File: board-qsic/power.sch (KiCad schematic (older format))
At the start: 43 parts, among them U306 AOZ3010PI, U307 AOZ3010PI, U308 RT8288A, U309 SC189, U401 XC7A75T-CSG324

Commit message: Reworked board from template.  Changed schematic to let me use the bus drivers and level converters more efficiently so to get all the signals.
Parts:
- removed C301, C302, C309, C310: 10uF, Capacitors_SMD:C_0603, symbol qsic-rescue:C_Small-device
- removed C303, C304: 2.2nF, Capacitors_SMD:C_0603, symbol qsic-rescue:C_Small-device
- removed C305, C306, C311, C312, C315, C317, C318, C320, C321, C323, C324, C326: 100nF, Capacitors_SMD:C_0603, symbol qsic-rescue:C_Small-device
- removed C307, C308, C313, C314: 22uF, Capacitors_SMD:C_0805, symbol qsic-rescue:C_Small-device
- removed D301: Configure, LEDs:LED-0603, symbol qsic-rescue:LED_Small_ALT
- removed L301, L302: 4.7uH, Resistors_SMD:R_0805, symbol qsic-rescue:L_Small-device
- removed L303: 1.5uH, Resistors_SMD:R_0805, symbol qsic-rescue:L_Small-device
- removed L304: 2.2uH, Resistors_SMD:R_0805, symbol qsic-rescue:L_Small-device
- removed R361: 240, Resistors_SMD:R_0603, symbol qsic-rescue:R-device
- removed R362, R363: 7.5k, Resistors_SMD:R_0603, symbol qsic-rescue:R-device
- removed R364: 31.1k, Resistors_SMD:R_0603, symbol qsic-rescue:R-device
- removed R365, R366: 10k, Resistors_SMD:R_0603, symbol qsic-rescue:R-device
- removed R367: 11.5k, Resistors_SMD:R_0603, symbol qsic-rescue:R-device
- removed R368: 100k, Resistors_SMD:R_0603, symbol qsic-rescue:R-device
- removed R369: 50k, Resistors_SMD:R_0603, symbol qsic-rescue:R-device
- removed R370: 18.2k, Resistors_SMD:R_0603, symbol qsic-rescue:R-device
- removed R371: 4.7k, Resistors_SMD:R_0603, symbol qsic-rescue:R-device
- removed U306, U307: AOZ3010PI, Housings_SOIC:SOIC-8-1EP_3.9x4.9mm_Pitch1.27mm, symbol myLib:AOZ3010PI
- removed U308: RT8288A, Housings_SOIC:SOIC-8-1EP_3.9x4.9mm_Pitch1.27mm, symbol myLib:RT8288A
- removed U309: SC189, TO_SOT_Packages_SMD:SOT-23-5, symbol myLib:SC189
- removed U401: XC7A75T-CSG324, myMods.pretty:CSG324, symbol myLib:XC7A75T-CSG324
- added C1201, C1203, C1205, C1207: 22uF, Capacitor_SMD:C_0805_2012Metric, symbol Device:CP1_Small
- added C1202, C1204, C1206, C1208: 10uF, Capacitor_SMD:C_0805_2012Metric, symbol Device:CP1_Small
- added R1201: 511k, Resistor_SMD:R_0603_1608Metric, symbol Device:R
- added R1202, R1205, R1208, R1211: 499k, Resistor_SMD:R_0603_1608Metric, symbol Device:R
- added R1203, R1206, R1209, R1212: 162k, Resistor_SMD:R_0603_1608Metric, symbol Device:R
- added R1204: 200k, Resistor_SMD:R_0603_1608Metric, symbol Device:R
- added R1207: 143k, Resistor_SMD:R_0603_1608Metric, symbol Device:R
- added R1210: 40.2, Resistor_SMD:R_0603_1608Metric, symbol Device:R
- added U101: XC7A75T-CSG324, Package_BGA:BGA-324_15.0x15.0mm_Layout18x18_P0.8mm_Ball0.5mm_Pad0.4mm_NSMD, symbol FPGA_Xilinx_Artix7:XC7A75T-CSG324
- added U1201, U1202, U1203, U1204: TPS82085, Package_LGA:Texas_SIL0008D_MicroSiP-8-1EP_2.8x3mm_P0.65mm_EP1.1x1.9mm_ThermalVias, symbol myLib:TPS82085
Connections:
- net labels added: 1V0, 1V5, 1V8, 3V3, 5V
- net labels removed: +1V0, +1V5, +1V8, +3V3, +5V
- wire segments 317 -> 240
- no-connect marks 4 -> 0
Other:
- note removed: "1.0V/4A"
- note removed: "1.5V/2A"
- note removed: "1.8V/1.5A"
- note removed: "3.3V/2A"

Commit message: Design of prototype is done.  Needs checking before sending out.
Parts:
- added C508, C512: 100nF, Capacitor_SMD:C_0603_1608Metric, symbol Device:C
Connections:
- net 1V0: now also C512.1
- net 1V8: now also C508.1
- net GND: now also U101.E8 (VCCBATT_0), C508.2, C512.2
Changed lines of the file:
@@
 $Descr A 11000 8500
 encoding utf-8
-Sheet 53 53
+Sheet 5 5
 Title "Power"
-Date "2019-09-30"
+Date "2019-10-07"
 Rev "0.2"
 Comp "QSIC - QBUS Storage & I/O Card"
@@
 $EndDescr
 Wire Wire Line
-	8875 1550 8875 1650
+	8875 1450 8875 1525
 Wire Wire Line
 	8775 1650 8875 1650
@@
 	6675 1950 6775 1950
 Wire Wire Line
-	6675 1600 6675 1650
+	6675 1425 6675 1525
 Wire Wire Line
 	6775 1650 6675 1650
@@
 Text HLabel 1125 1350 0    60   Input ~ 0
 5V
-Text Label 8875 1550 0    60   ~ 0
+Text Label 8875 1450 0    60   ~ 0
 1V0
-Text Label 6675 1600 2    60   ~ 0
+Text Label 6675 1425 2    60   ~ 0
 1V8
 Text HLabel 4050 1500 2    60   Output ~ 0
@@
 $EndComp
 Wire Wire Line
-	6775 2550 6700 2550
-Wire Wire Line
-	6700 2550 6700 2450
-Wire Wire Line
-	6775 2450 6700 2450
-Text Label 6575 2550 2    60   ~ 0
+	6775 2550 6750 2550
+Wire Wire Line
+	6750 2550 6750 2450
+Wire Wire Line
+	6775 2450 6750 2450
+Text Label 6700 2550 2    60   ~ 0
 1V0
 $Comp
@@
 	6475 2150 6775 2150
 Wire Wire Line
-	6575 2550 6700 2550
-Connection ~ 6700 2550
+	6700 2550 6750 2550
+Connection ~ 6750 2550
 $Comp
 L myLib:TPS82085 U1201
@@
 Connection ~ 1225 1500
 Connection ~ 1225 2750
+$Comp
+L Device:C C?
+U 1 1 5DDB3BFE
+P 9075 1700
+AR Path="/5DCB8CA6/5DDB3BFE" Ref="C?"  Part="1"
+AR Path="/5D96DF52/5DDB3BFE" Ref="C512"  Part="1"
+F 0 "C512" H 9190 1746 50  0000 L CNN
+F 1 "100nF" H 9190 1655 50  0000 L CNN
+F 2 "Capacitor_SMD:C_0603_1608Metric" H 9113 1550 50  0001 C CNN
+F 3 "~" H 9075 1700 50  0001 C CNN
+	1    9075 1700
+	1    0    0    -1
+$EndComp
+$Comp
+L Device:C C?
+U 1 1 5DDC711B
+P 6475 1700
+AR Path="/5DCB8CA6/5DDC711B" Ref="C?"  Part="1"
+AR Path="/5D96DF52/5DDC711B" Ref="C508"  Part="1"
+F 0 "C508" H 6361 1746 50  0000 R CNN
+F 1 "100nF" H 6361 1655 50  0000 R CNN
+F 2 "Capacitor_SMD:C_0603_1608Metric" H 6513 1550 50  0001 C CNN
+F 3 "~" H 6475 1700 50  0001 C CNN
+	1    6475 1700
+	1    0    0    -1
+$EndComp
+$Comp
+L power:GND #PWR?
+U 1 1 5DDDA595
+P 6475 1850
+AR Path="/5DCB8CA6/5DCBEACE/5DDDA595" Ref="#PWR?"  Part="1"
+AR Path="/5D96DF52/5DDDA595" Ref="#PWR0148"  Part="1"
+F 0 "#PWR0148" H 6475 1600 50  0001 C CNN
+F 1 "GND" H 6475 1700 50  0001 C CNN
+F 2 "" H 6475 1850 50  0000 C CNN
+F 3 "" H 6475 1850 50  0000 C CNN
+	1    6475 1850
+	1    0    0    -1
+$EndComp
+$Comp
+L power:GND #PWR?
+U 1 1 5DDDD3FE
+P 9075 1850
+AR Path="/5DCB8CA6/5DCBEACE/5DDDD3FE" Ref="#PWR?"  Part="1"
+AR Path="/5D96DF52/5DDDD3FE" Ref="#PWR0149"  Part="1"
+F 0 "#PWR0149" H 9075 1600 50  0001 C CNN
+F 1 "GND" H 9075 1700 50  0001 C CNN
+F 2 "" H 9075 1850 50  0000 C CNN
+F 3 "" H 9075 1850 50  0000 C CNN
+	1    9075 1850
+	1    0    0    -1
+$EndComp
+Wire Wire Line
+	9075 1550 9075 1525
+Wire Wire Line
+	9075 1525 8875 1525
+Connection ~ 8875 1525
+Wire Wire Line
+	8875 1525 8875 1650
+Wire Wire Line
+	6475 1550 6475 1525
+Wire Wire Line
+	6475 1525 6675 1525
+Connection ~ 6675 1525
+Wire Wire Line
+	6675 1525 6675 1650
+$Comp
+L power:GND #PWR?
+U 1 1 5DA43B10
+P 6475 2350
+AR Path="/5DCB8CA6/5DCBEACE/5DA43B10" Ref="#PWR?"  Part="1"
+AR Path="/5D96DF52/5DA43B10" Ref="#PWR?"  Part="1"
+F 0 "#PWR?" H 6475 2100 50  0001 C CNN
+F 1 "GND" H 6475 2200 50  0001 C CNN
+F 2 "" H 6475 2350 50  0000 C CNN
+F 3 "" H 6475 2350 50  0000 C CNN
+	1    6475 2350
+	-1   0    0    -1
+$EndComp
+Wire Wire Line
+	6475 2350 6775 2350
 $EndSCHEMATC

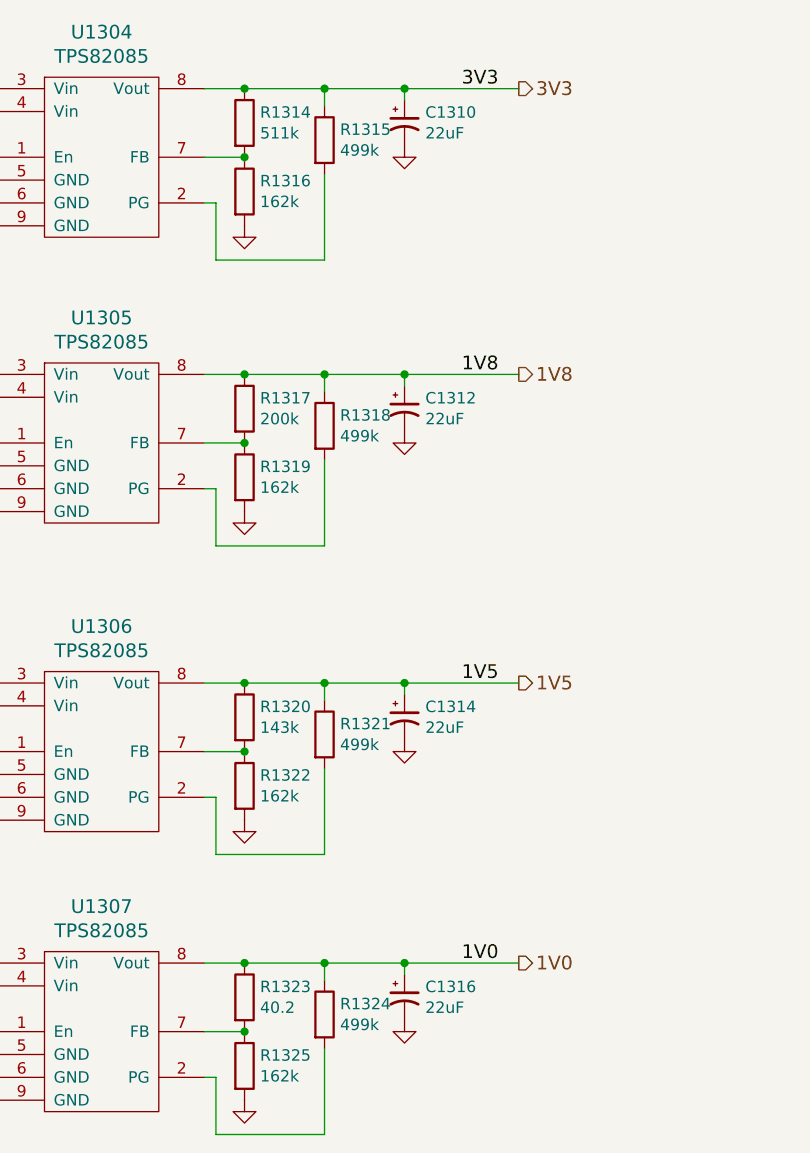
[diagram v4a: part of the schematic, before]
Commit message: Changes from Emanuel's comments.
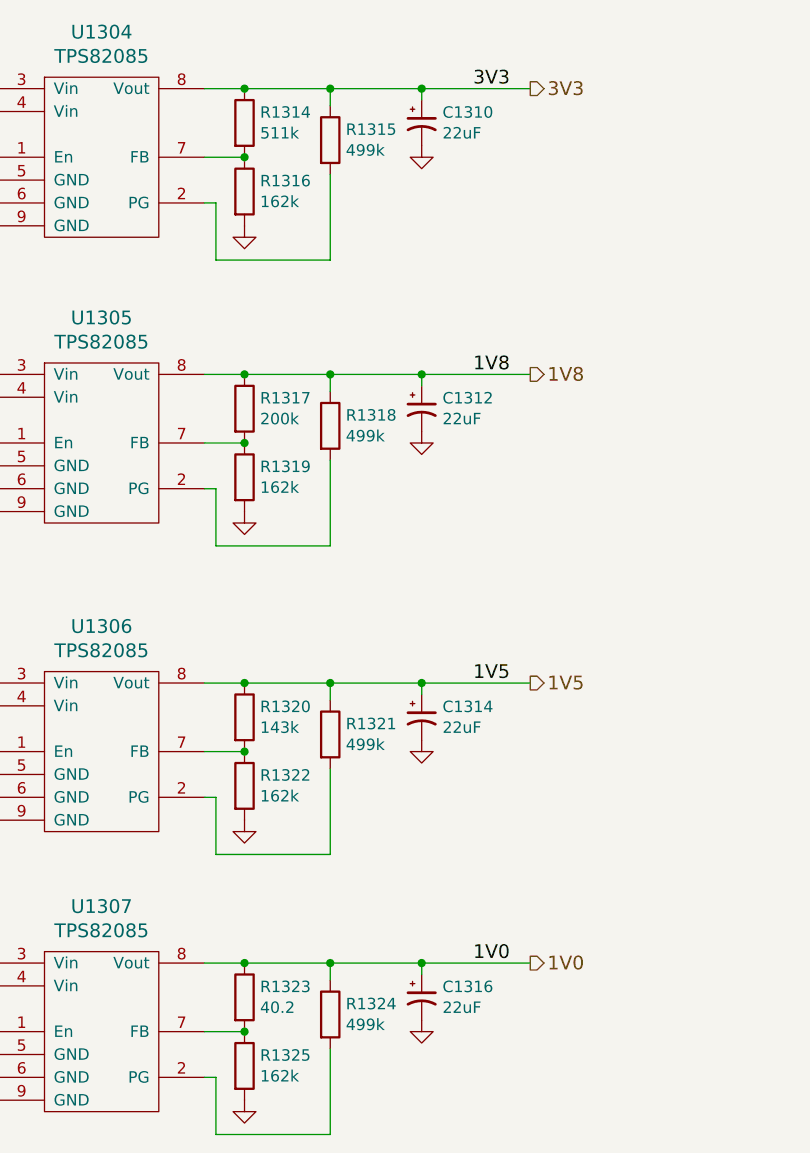
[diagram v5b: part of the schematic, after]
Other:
- moved on the sheet: C1310, C1312, C1314, C1316, R1315, R1318, R1321, R1324

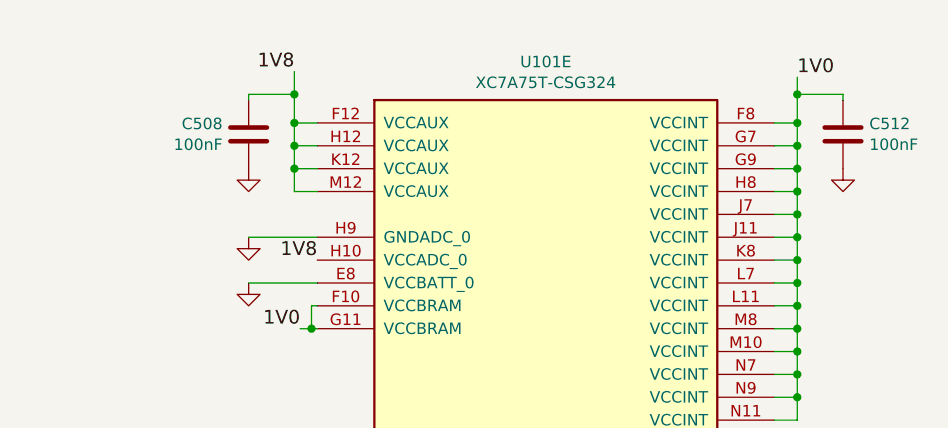
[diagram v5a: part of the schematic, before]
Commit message: Changed some capacitors from 100nF to 10uF
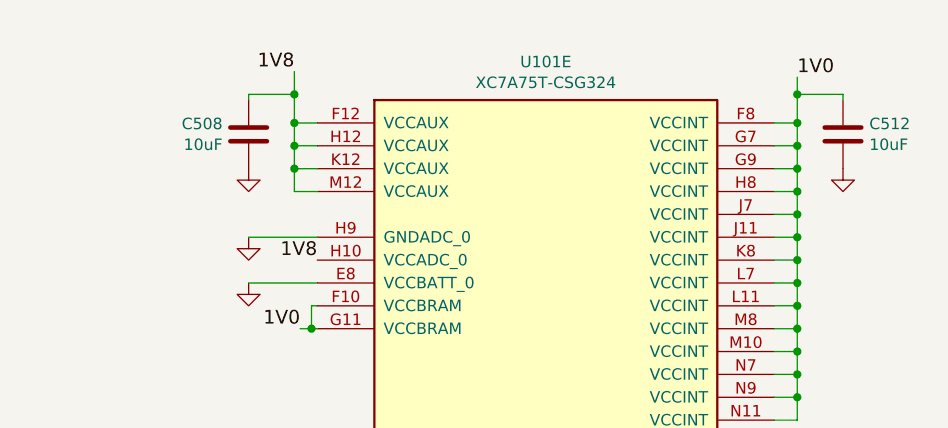
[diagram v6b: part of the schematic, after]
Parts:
- C508, C512: value 100nF -> 10uF
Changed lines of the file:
@@
 EESchema Schematic File Version 4
-LIBS:qsic-cache
 EELAYER 30 0
 EELAYER END
@@
 AR Path="/5D96DF52/5DDB3BFE" Ref="C512"  Part="1"
 F 0 "C512" H 9190 1746 50  0000 L CNN
-F 1 "100nF" H 9190 1655 50  0000 L CNN
+F 1 "10uF" H 9190 1655 50  0000 L CNN
 F 2 "Capacitor_SMD:C_0603_1608Metric" H 9113 1550 50  0001 C CNN
 F 3 "~" H 9075 1700 50  0001 C CNN
@@
 AR Path="/5D96DF52/5DDC711B" Ref="C508"  Part="1"
 F 0 "C508" H 6361 1746 50  0000 R CNN
-F 1 "100nF" H 6361 1655 50  0000 R CNN
+F 1 "10uF" H 6361 1655 50  0000 R CNN
 F 2 "Capacitor_SMD:C_0603_1608Metric" H 6513 1550 50  0001 C CNN
 F 3 "~" H 6475 1700 50  0001 C CNN

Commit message: These are all old changes in directories that are now historical.
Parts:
- C1201, C1203, C1205, C1207: value 22uF -> 22µF
- C1202, C1204, C1206, C1208, C508, C512: value 10uF -> 10µF
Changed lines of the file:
@@
 AR Path="/5D96DF52/5D81EC1E" Ref="C1310"  Part="1"
 F 0 "C1310" H 3716 1696 50  0000 L CNN
-F 1 "22uF" H 3716 1605 50  0000 L CNN
+F 1 "22µF" H 3716 1605 50  0000 L CNN
 F 2 "Capacitor_SMD:C_0805_2012Metric" H 3625 1650 50  0001 C CNN
 F 3 "~" H 3625 1650 50  0001 C CNN
@@
 AR Path="/5D96DF52/5D81F508" Ref="C1311"  Part="1"
 F 0 "C1311" H 1485 1721 50  0000 R CNN
-F 1 "10uF" H 1485 1630 50  0000 R CNN
+F 1 "10µF" H 1485 1630 50  0000 R CNN
 F 2 "Capacitor_SMD:C_0805_2012Metric" H 1575 1675 50  0001 C CNN
 F 3 "~" H 1575 1675 50  0001 C CNN
@@
 AR Path="/5D96DF52/5DB64088" Ref="C1312"  Part="1"
 F 0 "C1312" H 3716 2946 50  0000 L CNN
-F 1 "22uF" H 3716 2855 50  0000 L CNN
+F 1 "22µF" H 3716 2855 50  0000 L CNN
 F 2 "Capacitor_SMD:C_0805_2012Metric" H 3625 2900 50  0001 C CNN
 F 3 "~" H 3625 2900 50  0001 C CNN
@@
 AR Path="/5D96DF52/5DB6408E" Ref="C1313"  Part="1"
 F 0 "C1313" H 1485 2971 50  0000 R CNN
-F 1 "10uF" H 1485 2880 50  0000 R CNN
+F 1 "10µF" H 1485 2880 50  0000 R CNN
 F 2 "Capacitor_SMD:C_0805_2012Metric" H 1575 2925 50  0001 C CNN
 F 3 "~" H 1575 2925 50  0001 C CNN
@@
 AR Path="/5D96DF52/5DB87EC1" Ref="C1314"  Part="1"
 F 0 "C1314" H 3716 4296 50  0000 L CNN
-F 1 "22uF" H 3716 4205 50  0000 L CNN
+F 1 "22µF" H 3716 4205 50  0000 L CNN
 F 2 "Capacitor_SMD:C_0805_2012Metric" H 3625 4250 50  0001 C CNN
 F 3 "~" H 3625 4250 50  0001 C CNN
@@
 AR Path="/5D96DF52/5DB87EC7" Ref="C1315"  Part="1"
 F 0 "C1315" H 1485 4321 50  0000 R CNN
-F 1 "10uF" H 1485 4230 50  0000 R CNN
+F 1 "10µF" H 1485 4230 50  0000 R CNN
 F 2 "Capacitor_SMD:C_0805_2012Metric" H 1575 4275 50  0001 C CNN
 F 3 "~" H 1575 4275 50  0001 C CNN
@@
 AR Path="/5D96DF52/5DBB2B9B" Ref="C1316"  Part="1"
 F 0 "C1316" H 3716 5521 50  0000 L CNN
-F 1 "22uF" H 3716 5430 50  0000 L CNN
+F 1 "22µF" H 3716 5430 50  0000 L CNN
 F 2 "Capacitor_SMD:C_0805_2012Metric" H 3625 5475 50  0001 C CNN
 F 3 "~" H 3625 5475 50  0001 C CNN
@@
 AR Path="/5D96DF52/5DBB2BA1" Ref="C1317"  Part="1"
 F 0 "C1317" H 1485 5546 50  0000 R CNN
-F 1 "10uF" H 1485 5455 50  0000 R CNN
+F 1 "10µF" H 1485 5455 50  0000 R CNN
 F 2 "Capacitor_SMD:C_0805_2012Metric" H 1575 5500 50  0001 C CNN
 F 3 "~" H 1575 5500 50  0001 C CNN
@@
 AR Path="/5D96DF52/5DDB3BFE" Ref="C512"  Part="1"
 F 0 "C512" H 9190 1746 50  0000 L CNN
-F 1 "10uF" H 9190 1655 50  0000 L CNN
+F 1 "10µF" H 9190 1655 50  0000 L CNN
 F 2 "Capacitor_SMD:C_0603_1608Metric" H 9113 1550 50  0001 C CNN
 F 3 "~" H 9075 1700 50  0001 C CNN
@@
 AR Path="/5D96DF52/5DDC711B" Ref="C508"  Part="1"
 F 0 "C508" H 6361 1746 50  0000 R CNN
-F 1 "10uF" H 6361 1655 50  0000 R CNN
+F 1 "10µF" H 6361 1655 50  0000 R CNN
 F 2 "Capacitor_SMD:C_0603_1608Metric" H 6513 1550 50  0001 C CNN
 F 3 "~" H 6475 1700 50  0001 C CNN
